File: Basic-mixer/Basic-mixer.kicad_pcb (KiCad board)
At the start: 2 copper layers, 82 x 133 mm, 37 parts, among them J1 In, J2 Power Input, J3 In, J4 Out, J5 In, J6 In, SW1 Mute, SW2 Mute, SW3 Mute, SW4 Mute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

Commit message: finish basic mixer pcb
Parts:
- moved R8 230.5 mm to (44.4, 130.0)
- moved U1 228.6 mm to (32.7, 132.8), turned to 90 degrees
- moved R9 228.2 mm to (44.4, 123.0)
- moved R7 221.4 mm to (54.6, 126.5), turned to 180 degrees
- moved C5 200.6 mm to (67.0, 137.0), turned to -90 degrees
- moved C2 190.1 mm to (32.0, 120.5)
- moved C3 180.7 mm to (36.5, 137.5)
- moved J2 8.68 mm to (43.9, 135.7)
- moved J4 2.43 mm to (61.0, 122.0)
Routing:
- net (no net): vias 12 -> 13
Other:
- board size 82 x 133 mm -> 82 x 128 mm
- board text added: "Audio mixer"
- board text added: "V1.0 BleepSound 2022"
- board text removed: "Board 1/2"
- board text removed: "Snare + HiHat V1.0 BleepSound 2022"

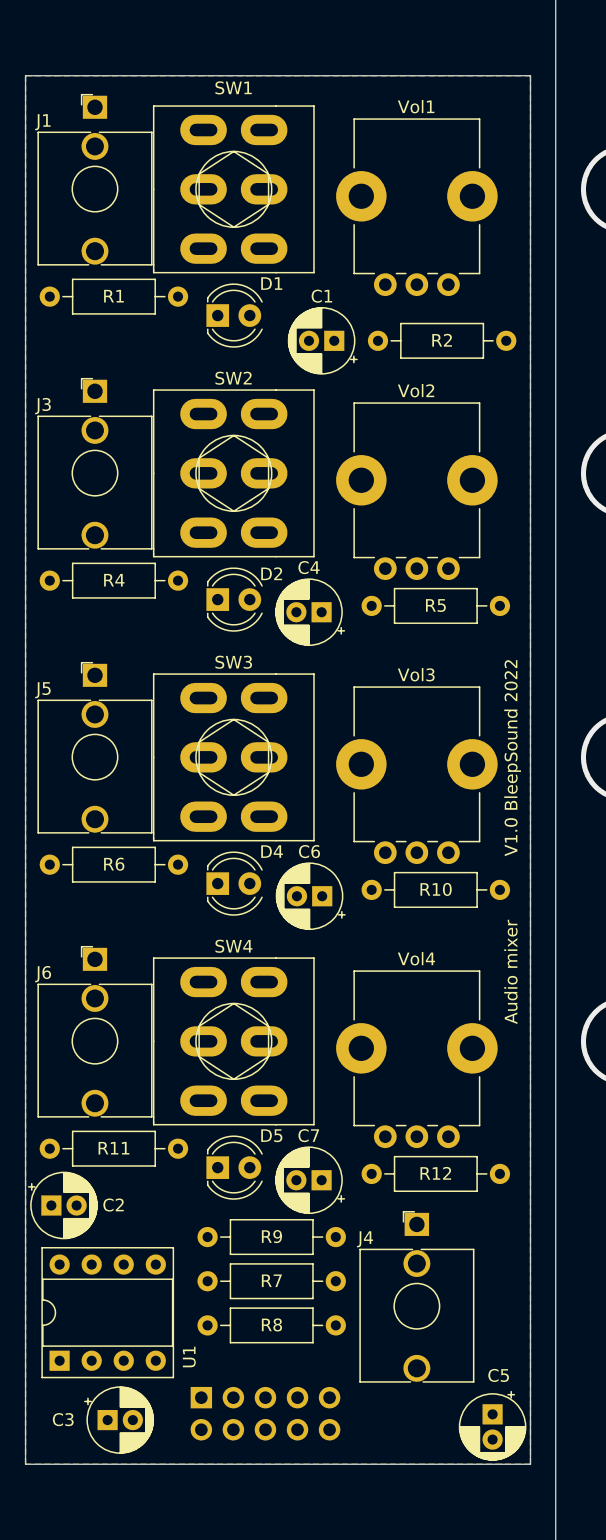
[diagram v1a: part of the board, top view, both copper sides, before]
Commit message: Finished pcb for basic mixer
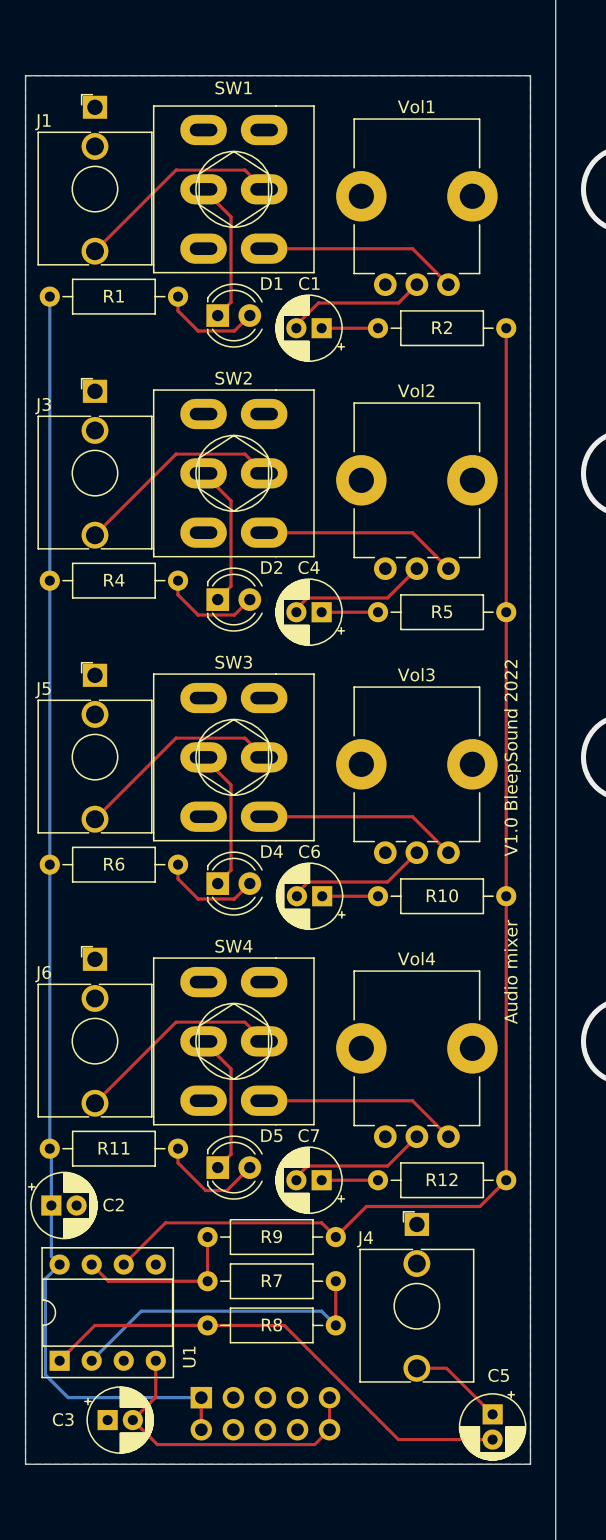
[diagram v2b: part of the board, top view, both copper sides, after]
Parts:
- moved C1 1.41 mm to (53.5, 51.0)
- moved R2 1.00 mm to (68.1, 51.0)
- moved R10 0.71 mm to (68.1, 96.0)
- moved R12 0.71 mm to (68.1, 118.5)
- moved R5 0.71 mm to (68.1, 73.5)
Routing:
- net +12V: track 0.00 -> 101.8 mm
- net Net-(R10-Pad1): track 0.00 -> 101.5 mm
- net Net-(C5-Pad2): track 0.00 -> 39.2 mm
- net Net-(R7-Pad1): track 0.00 -> 24.9 mm
- net -12V: track 0.00 -> 24.9 mm
- net Net-(J3-PadT): track 0.00 -> 16.7 mm
- net Net-(J1-PadT): track 0.00 -> 16.7 mm
- net Net-(J6-PadT): track 0.00 -> 16.7 mm
- net Net-(J5-PadT): track 0.00 -> 16.7 mm
- net Net-(SW4-Pad6): track 0.00 -> 15.8 mm
- net Net-(SW3-Pad6): track 0.00 -> 15.8 mm
- net Net-(SW2-Pad6): track 0.00 -> 15.8 mm
- net Net-(SW1-Pad6): track 0.00 -> 15.8 mm
- net Net-(R7-Pad2): track 0.00 -> 13.2 mm
- net Net-(D5-Pad1): track 0.00 -> 11.3 mm
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- removed copper zone on F.Cu, net GND
